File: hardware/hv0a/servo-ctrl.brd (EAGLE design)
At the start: 120 x 100 mm, 264 parts, among them J201 SH-5, J202 SH-5, J203 SH-5, J204 SH-5, J205 SH-5, J301 2P-6.35P, J302 2P-6.35P, J401 4P-6.35P, J402 SH-2, J403 2P-6.35P, J501 SH-6, J502 SH-3, J503 USB-SHIELD, J504 SH-2, J505 F20F-10DP-1V, J506 SH-3, P301 POWPAD, P302 POWPAD, P401 POWPAD, P402 POWPAD, P403 POWPAD, P404 POWPAD, P405 POWPAD, P406 POWPAD, Q401 IRF7580, Q402 IRF7580, Q403 IRF7580, Q404 IRF7580, Q405 IRF7580, Q406 IRF7580, Q407 IRF7580, Q408 IRF7580, Q409 IRF7580, U101 DSC1101, U102 TMC4671, U201 SRV05-4, U202 SRV05-4, U203 SRV05-4, U204 SRV05-4, U205 74LVC3G17, U206 74LVC3G17, U207 74LVC3G17, U208 74LVC3G17, U301 MIC4682, U302 MIC39101, U303 MIC39101, U401 SI82397, U402 SI82397, U403 SI82397, U404 SI82397, U405 AD8418A, U406 AD8418A, U407 SI8261, U501 CP2130/2102N

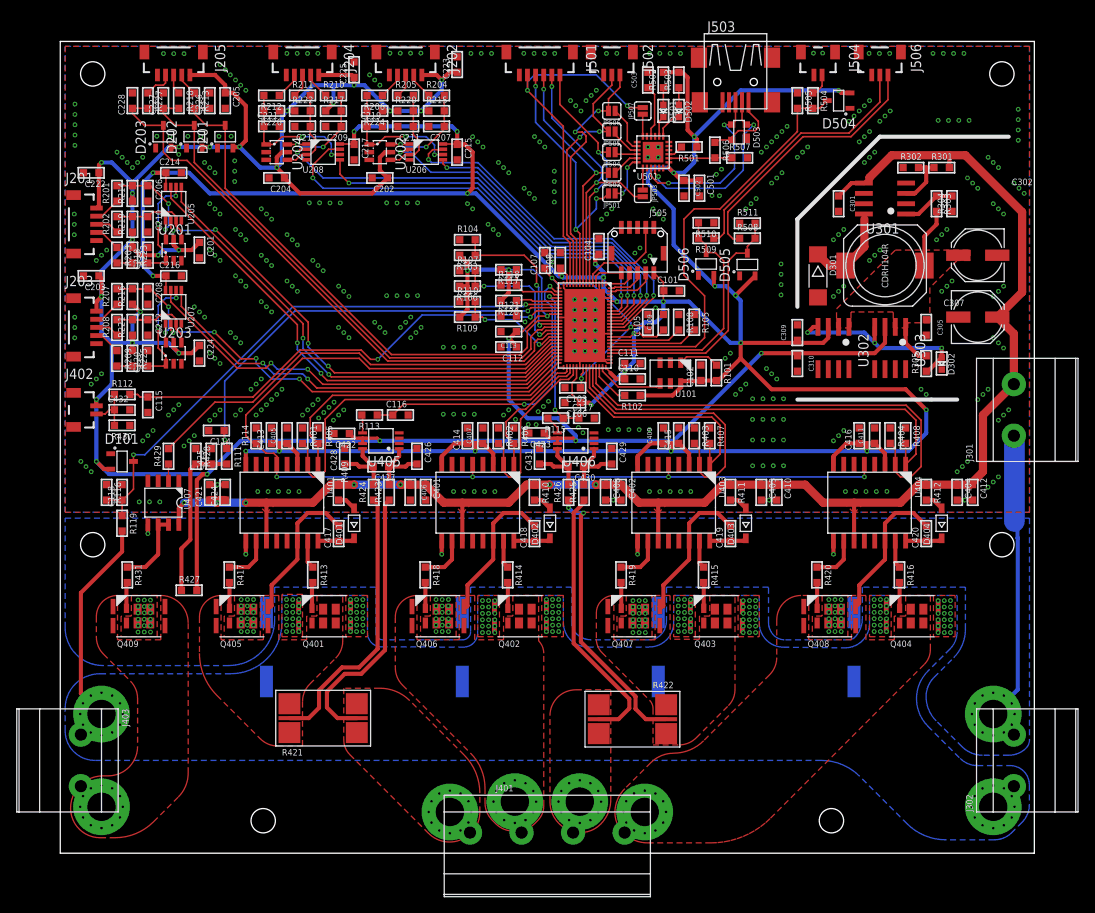
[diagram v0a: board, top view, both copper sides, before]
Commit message: finished pcb, added pdf and png exports of pcb
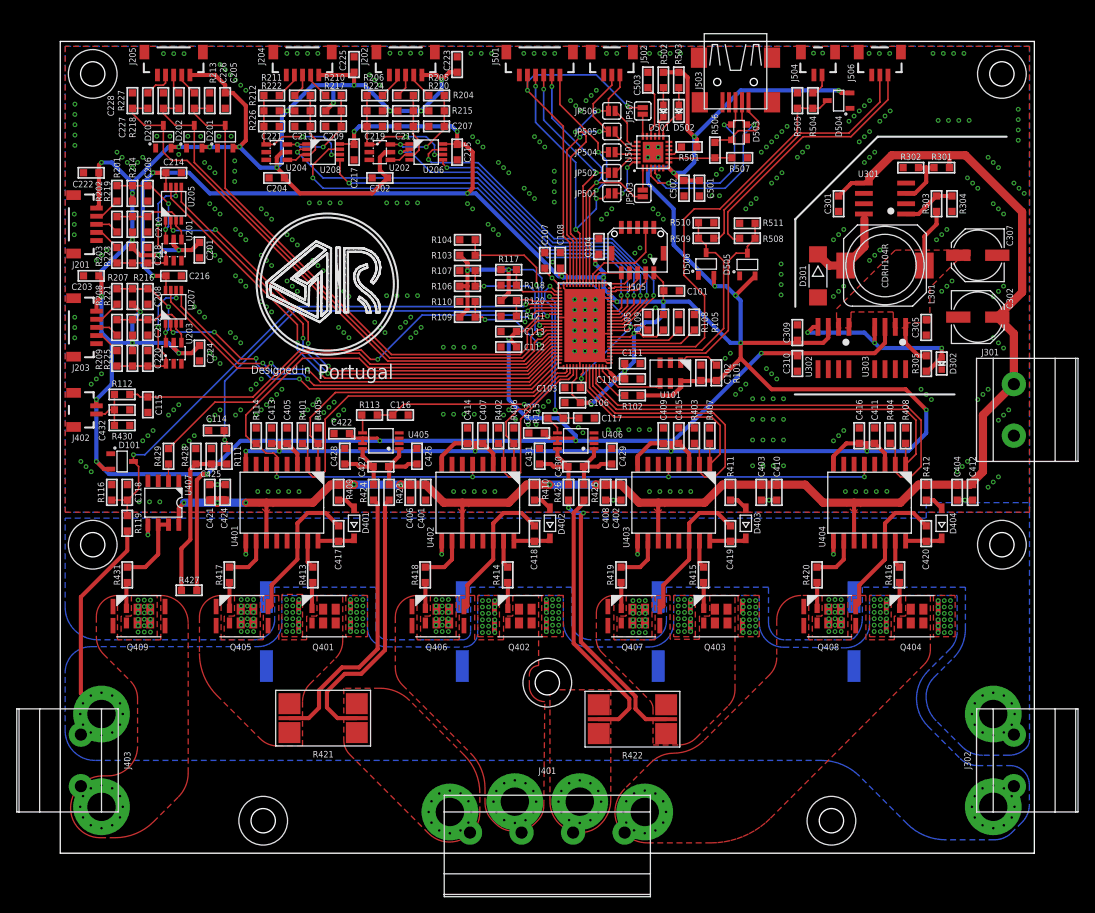
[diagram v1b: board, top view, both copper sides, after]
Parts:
- added U$1: (no value), Utility > Silkscreen:RAFAEL_SILVA_10MM_CIRCLE
- moved C303 1.91 mm to (97.8, 27.3)
- moved C304 1.91 mm to (73.7, 27.3)
- moved C306 1.91 mm to (49.5, 27.3)
- moved C308 1.91 mm to (25.4, 27.3)
- moved C225 0.64 mm to (36.2, 97.2)
- moved C118 0.64 mm to (8.26, 44.5)
- moved R119 0.64 mm to (8.26, 40.6)
- moved R116 0.63 mm to (6.35, 44.5)
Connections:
- net N$1 renamed WY1@J401
- net N$29 renamed UX1@J401
- net N$33 renamed STEP@J
- net N$59 renamed DIR@J
- net N$61 renamed PWM_IN@J
- net N$71 renamed ENC_A@J
- net N$72 renamed ENC_B@J
- net N$73 renamed ENC_N@J
- net N$76 renamed ENC_2_A@J
- net N$77 renamed ENC_2_B@J
- net N$78 renamed ENC_2_N@J
- net N$82 renamed HALL_WY@J
- net N$83 renamed HALL_V@J
- net N$84 renamed HALL_UX@J
- net N$88 renamed REF_R@J
- net N$89 renamed REF_H@J
- net N$90 renamed REF_L@J
- net N$97 renamed AENC_WY@J
- net N$98 renamed AENC_VN@J
- net N$99 renamed AENC_UX@J
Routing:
- net GND: track 83.3 -> 47.7 mm
- net 5V: track 389.7 -> 390.4 mm
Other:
- board text added: "!CS"
- board text added: "12V"
- board text added: "5V"
- board text added: "A"
- board text added: "AENCODER"
- board text added: "B"
- board text added: "BRAKE"
- board text added: "DC IN"
- board text added: "DC MOTOR"
- board text added: "DCBUS"
- board text added: "DIR"
- board text added: "Designed in"
- board text added: "ENCODER"
- board text added: "ENCODER 2"
- board text added: "GND"
- board text added: "H"
- board text added: "HALL"
- board text added: "INT"
- board text added: "L"
- board text added: "MISO"
- board text added: "MOSI"
- board text added: "N"
- board text added: "PHASE OUT"
- board text added: "PWM"
- board text added: "PWM IN"
- board text added: "Portugal"
- board text added: "R"
- board text added: "REF SW"
- board text added: "RX"
- board text added: "SCK"
- board text added: "SPI"
- board text added: "STEP"
- board text added: "STEP DIR"
- board text added: "T"
- board text added: "T MOTOR"
- board text added: "TX"
- board text added: "UART"
- board text added: "USB"
- board text added: "UX"
- board text added: "UX1"
- board text added: "V"
- board text added: "VN"
- board text added: "VX2"
- board text added: "WY"
- board text added: "WY1"
- board text added: "Y2"
- board text removed: "TODO: Silkscreen identifiers labels etc logos silckscreen names add test points heatsink/ heatsink mounting"

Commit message: bom
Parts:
- C118: value 10n -> 100p

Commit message: component request preparation
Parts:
- C111: value 470n -> 4u7
- R428: value 1k13 -> 1k2
- R430: value 10k -> 1k2
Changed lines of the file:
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@@
 <drawing>
 <settings>
-<setting alwaysvectorfont="yes"/>
+<setting alwaysvectorfont="no"/>
 <setting verticaltext="up"/>
 </settings>
@@
 <attribute name="NAME" x="21.336" y="96.139" size="0.8" layer="25" font="vector" ratio="15" rot="R270" align="center"/>
 </element>
-<element name="C111" library="Passive Components &gt; Capacitors &gt; Multilayer Ceramic Capacitors MLCC" package="0603_WAVE" value="470n" x="70.485" y="60.325" smashed="yes">
+<element name="C111" library="Passive Components &gt; Capacitors &gt; Multilayer Ceramic Capacitors MLCC" package="0603_WAVE" value="4u7" x="70.485" y="60.325" smashed="yes">
 <attribute name="NAME" x="70.485" y="61.6585" size="0.8" layer="25" font="vector" ratio="15" align="center"/>
 </element>
@@
 <attribute name="NAME" x="76.3905" y="75.692" size="0.8" layer="25" font="vector" ratio="15" rot="R180" align="center"/>
 </element>
-<element name="R428" library="Passive Components &gt; Resistors &gt; Chip Resistors" package="0603_WAVE" value="1k13" x="16.7005" y="48.895" smashed="yes" rot="R270">
+<element name="R428" library="Passive Components &gt; Resistors &gt; Chip Resistors" package="0603_WAVE" value="1k2" x="16.7005" y="48.895" smashed="yes" rot="R270">
 <attribute name="NAME" x="15.367" y="48.895" size="0.8" layer="25" font="vector" ratio="15" rot="R270" align="center"/>
 </element>
-<element name="R430" library="Passive Components &gt; Resistors &gt; Chip Resistors" package="0603_WAVE" value="10k" x="7.62" y="52.705" smashed="yes" rot="R180">
+<element name="R430" library="Passive Components &gt; Resistors &gt; Chip Resistors" package="0603_WAVE" value="1k2" x="7.62" y="52.705" smashed="yes" rot="R180">
 <attribute name="NAME" x="7.62" y="51.3715" size="0.8" layer="25" font="vector" ratio="15" rot="R180" align="center"/>
 </element>

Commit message: component request
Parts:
- R504, R508, R509: value 24k -> 100
- R505, R510, R511: value 24k -> 10k
- R506: value 24k -> 5k
- R507: value 47k -> 10k
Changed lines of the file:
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@@
 <attribute name="NAME" x="77.47" y="85.725" size="0.8" layer="25" font="vector" ratio="15" rot="R180" align="center"/>
 </element>
-<element name="R506" library="Passive Components &gt; Resistors &gt; Chip Resistors" package="0603_WAVE" value="24k" x="80.645" y="86.614" smashed="yes" rot="R270">
+<element name="R506" library="Passive Components &gt; Resistors &gt; Chip Resistors" package="0603_WAVE" value="5k" x="80.645" y="86.614" smashed="yes" rot="R270">
 <attribute name="NAME" x="80.645" y="89.789" size="0.8" layer="25" font="vector" ratio="15" rot="R270" align="center"/>
 </element>
-<element name="R507" library="Passive Components &gt; Resistors &gt; Chip Resistors" package="0603_WAVE" value="47k" x="83.693" y="85.6615" smashed="yes">
+<element name="R507" library="Passive Components &gt; Resistors &gt; Chip Resistors" package="0603_WAVE" value="10k" x="83.693" y="85.6615" smashed="yes">
 <attribute name="NAME" x="83.693" y="84.328" size="0.8" layer="25" font="vector" ratio="15" align="center"/>
 </element>
@@
 <attribute name="NAME" x="43.688" y="34.29" size="0.8" layer="25" font="vector" ratio="15" rot="R270" align="center"/>
 </element>
-<element name="R508" library="Passive Components &gt; Resistors &gt; Chip Resistors" package="0603_WAVE" value="24k" x="84.6455" y="75.7555" smashed="yes">
+<element name="R508" library="Passive Components &gt; Resistors &gt; Chip Resistors" package="0603_WAVE" value="100" x="84.6455" y="75.7555" smashed="yes">
 <attribute name="NAME" x="87.8205" y="75.692" size="0.8" layer="25" font="vector" ratio="15" align="center"/>
 </element>
-<element name="R509" library="Passive Components &gt; Resistors &gt; Chip Resistors" package="0603_WAVE" value="24k" x="79.5655" y="75.7555" smashed="yes" rot="R180">
+<element name="R509" library="Passive Components &gt; Resistors &gt; Chip Resistors" package="0603_WAVE" value="100" x="79.5655" y="75.7555" smashed="yes" rot="R180">
 <attribute name="NAME" x="76.3905" y="75.692" size="0.8" layer="25" font="vector" ratio="15" rot="R180" align="center"/>
 </element>
@@
 <attribute name="NAME" x="12.0015" y="48.895" size="0.8" layer="25" font="vector" ratio="15" rot="R90" align="center"/>
 </element>
-<element name="R510" library="Passive Components &gt; Resistors &gt; Chip Resistors" package="0603_WAVE" value="24k" x="79.5655" y="77.6605" smashed="yes" rot="R180">
+<element name="R510" library="Passive Components &gt; Resistors &gt; Chip Resistors" package="0603_WAVE" value="10k" x="79.5655" y="77.6605" smashed="yes" rot="R180">
 <attribute name="NAME" x="76.3905" y="77.724" size="0.8" layer="25" font="vector" ratio="15" rot="R180" align="center"/>
 </element>
@@
 <attribute name="NAME" x="32.385" y="12.192" size="0.8" layer="21" font="vector" ratio="15" align="center"/>
 </element>
-<element name="R511" library="Passive Components &gt; Resistors &gt; Chip Resistors" package="0603_WAVE" value="24k" x="84.6455" y="77.597" smashed="yes">
+<element name="R511" library="Passive Components &gt; Resistors &gt; Chip Resistors" package="0603_WAVE" value="10k" x="84.6455" y="77.597" smashed="yes">
 <attribute name="NAME" x="87.8205" y="77.6605" size="0.8" layer="25" font="vector" ratio="15" align="center"/>
 </element>
-<element name="R504" library="Passive Components &gt; Resistors &gt; Chip Resistors" package="0603_WAVE" value="24k" x="92.71" y="92.71" smashed="yes" rot="R270">
+<element name="R504" library="Passive Components &gt; Resistors &gt; Chip Resistors" package="0603_WAVE" value="100" x="92.71" y="92.71" smashed="yes" rot="R270">
 <attribute name="NAME" x="92.71" y="89.535" size="0.8" layer="25" font="vector" ratio="15" rot="R270" align="center"/>
 </element>
-<element name="R505" library="Passive Components &gt; Resistors &gt; Chip Resistors" package="0603_WAVE" value="24k" x="90.805" y="92.71" smashed="yes" rot="R270">
+<element name="R505" library="Passive Components &gt; Resistors &gt; Chip Resistors" package="0603_WAVE" value="10k" x="90.805" y="92.71" smashed="yes" rot="R270">
 <attribute name="NAME" x="90.805" y="89.535" size="0.8" layer="25" font="vector" ratio="15" rot="R270" align="center"/>
 </element>
